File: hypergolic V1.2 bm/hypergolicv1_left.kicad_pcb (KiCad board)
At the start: 2 copper layers, 119.9 x 87.7 mm, 25 parts, among them SW10 SW_Push, SW11 SW_Push, SW12 SW_Push, SW14 SW_Push, SW15 SW_Push, SW16 SW_Push, SW17 SW_Push, SW18 SW_Push, SW2 SW_Push, SW20 SW_Push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

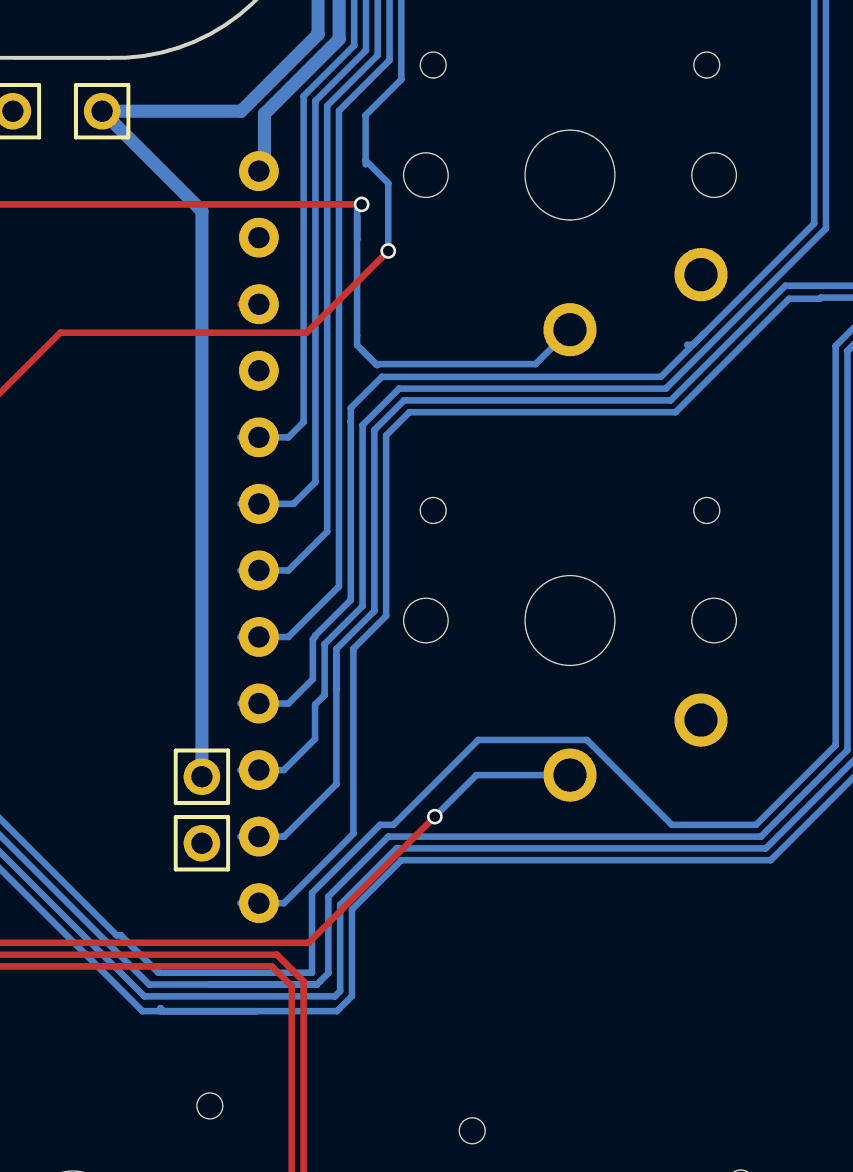
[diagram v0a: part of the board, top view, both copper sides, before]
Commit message: More trace corrections
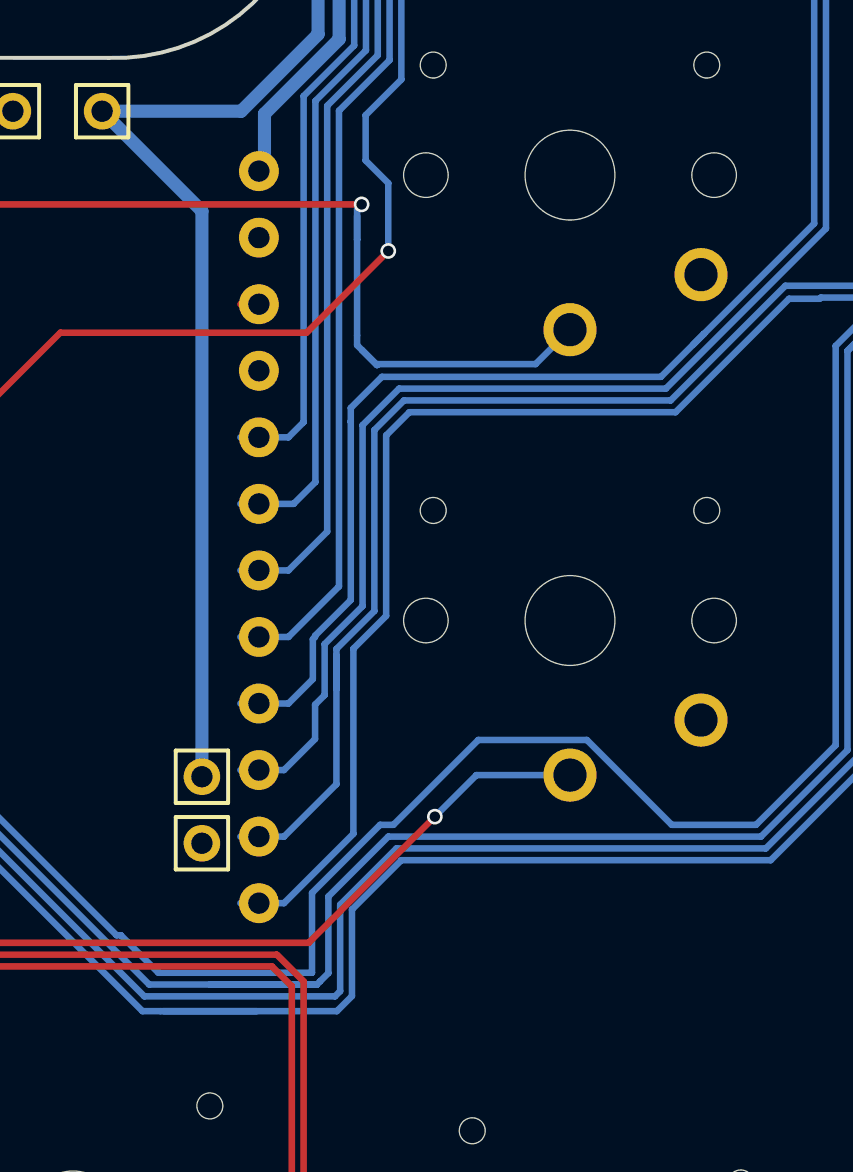
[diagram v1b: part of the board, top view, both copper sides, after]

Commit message: Add silkscreen to hypergolic
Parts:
- added REF**: silk_pg1232_footprint, silkscreens:pg1232_footprint, F.Cu at (95.8, 92.0)

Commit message: Swap silkscreen, add gerbers
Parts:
- removed the REF** at (95.8, 92.0)
- added REF**: silk_pg2132_top, silkscreens:pg1232_top, F.Cu at (83.3, 92.7)
- added REF**: silk_pg1232_bottom, silkscreens:pg1232_bottom, F.Cu at (102.6, 92.7)
